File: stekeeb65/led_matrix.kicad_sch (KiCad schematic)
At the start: 68 parts

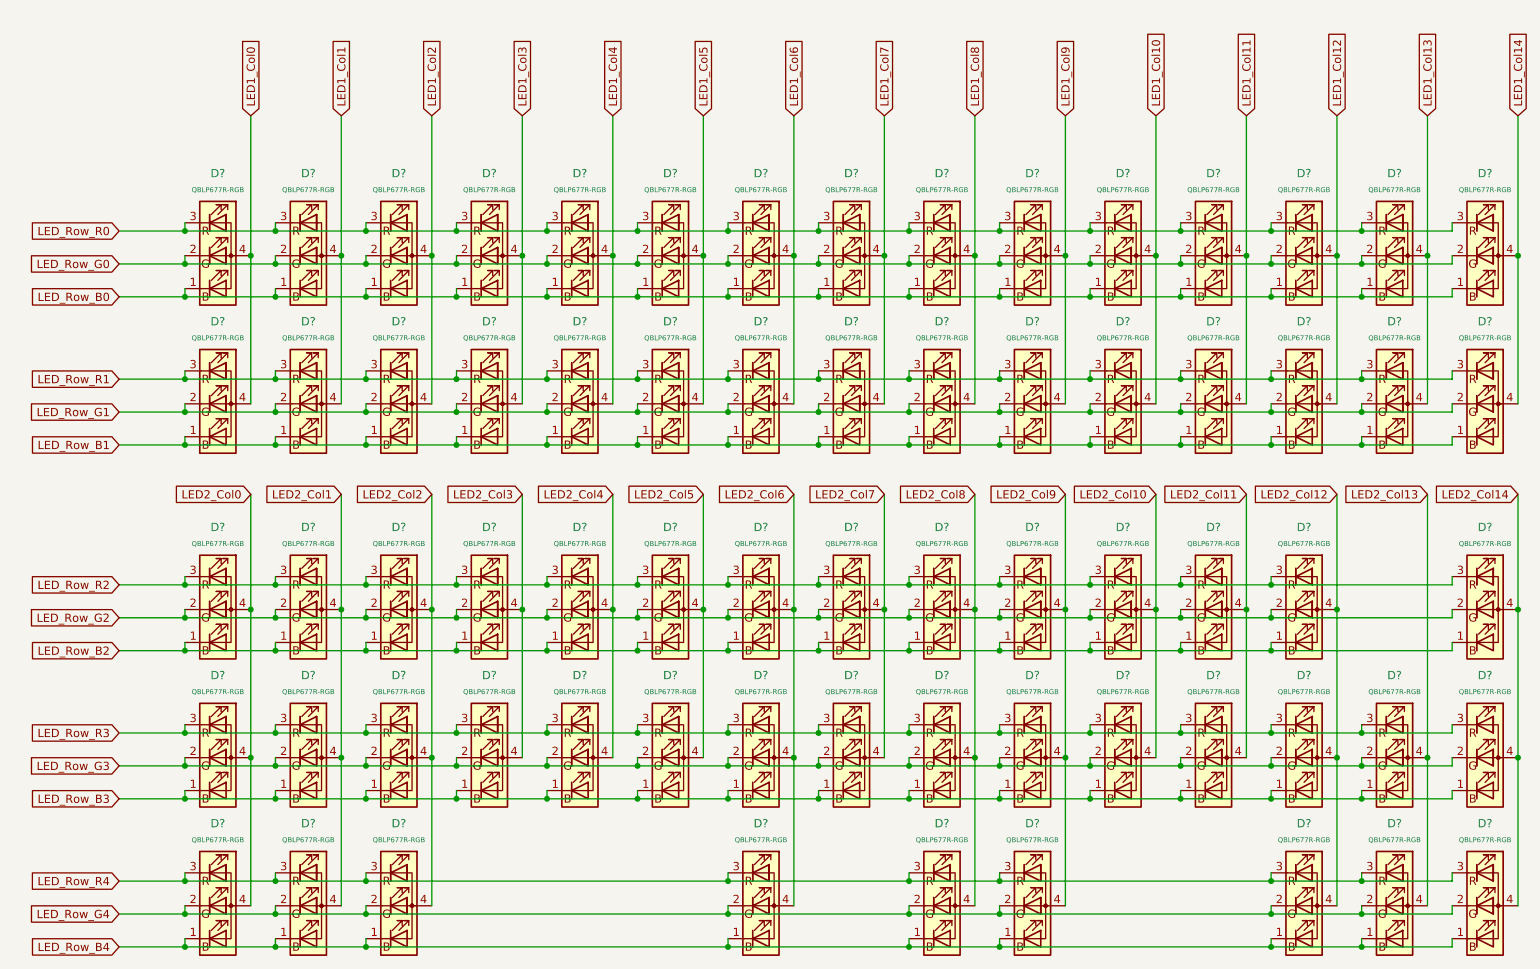
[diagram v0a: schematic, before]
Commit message: Adding keyboard footprints
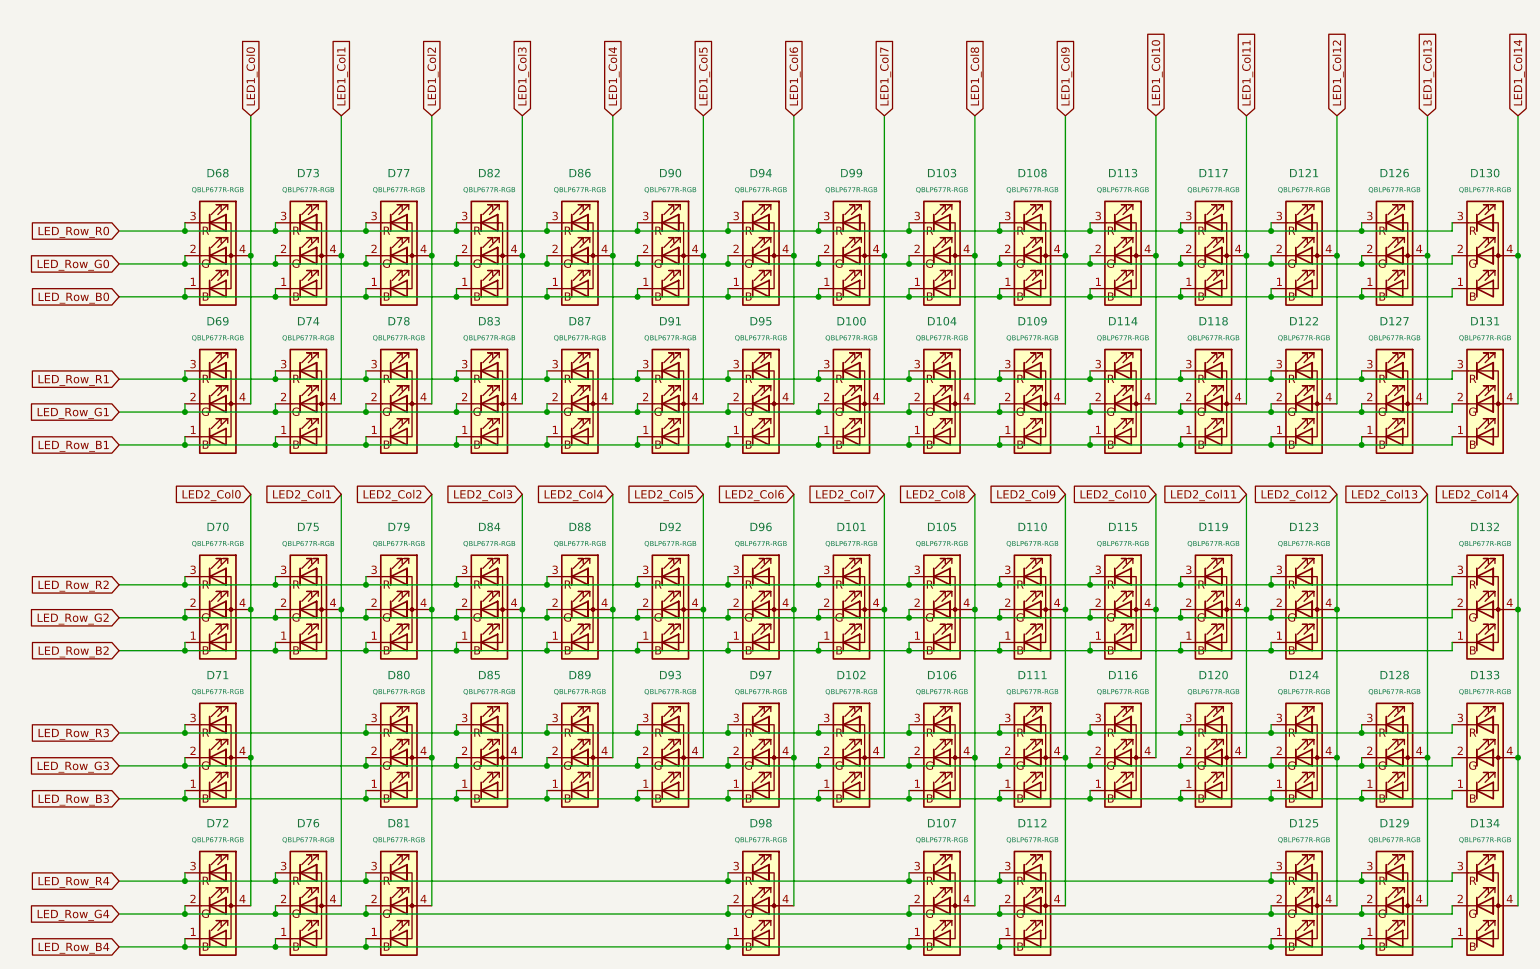
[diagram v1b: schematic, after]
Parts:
- removed D?: QBLP677R-RGB, symbol Device:LED_BGRA
- D100, D101, D102, D103, D104, D105, D106, D107, D108, D109, D110, D111, D112, D113, D114, D115, D116, D117, D118, D119, D120, D121, D122, D123, D124, D125, D126, D127, D128, D129, D130, D131, D132, D133, D134, D68, D69, D70, D71, D72, D73, D74, D75, D76, D77, D78, D79, D80, D81, D82, D83, D84, D85, D86, D87, D88, D89, D90, D91, D92, D93, D94, D95, D96, D97, D98, D99: renamed from D?; footprint (none) -> SamacSys_Parts:QBLP677R-RGB

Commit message: Committing before changes to PCB
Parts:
- D100, D101, D102, D103, D104, D105, D106, D107, D108, D109, D110, D111, D112, D113, D114, D115, D116, D117, D118, D119, D120, D121, D122, D123, D124, D125, D126, D127, D128, D129, D130, D131, D132, D133, D134, D68, D69, D70, D71, D72, D73, D74, D75, D76, D77, D78, D79, D80, D81, D82, D83, D84, D85, D86, D87, D88, D89, D90, D91, D92, D93, D94, D95, D96, D97, D98, D99: footprint SamacSys_Parts:QBLP677R-RGB -> random-keyboard-parts:QBLP677R-RGB

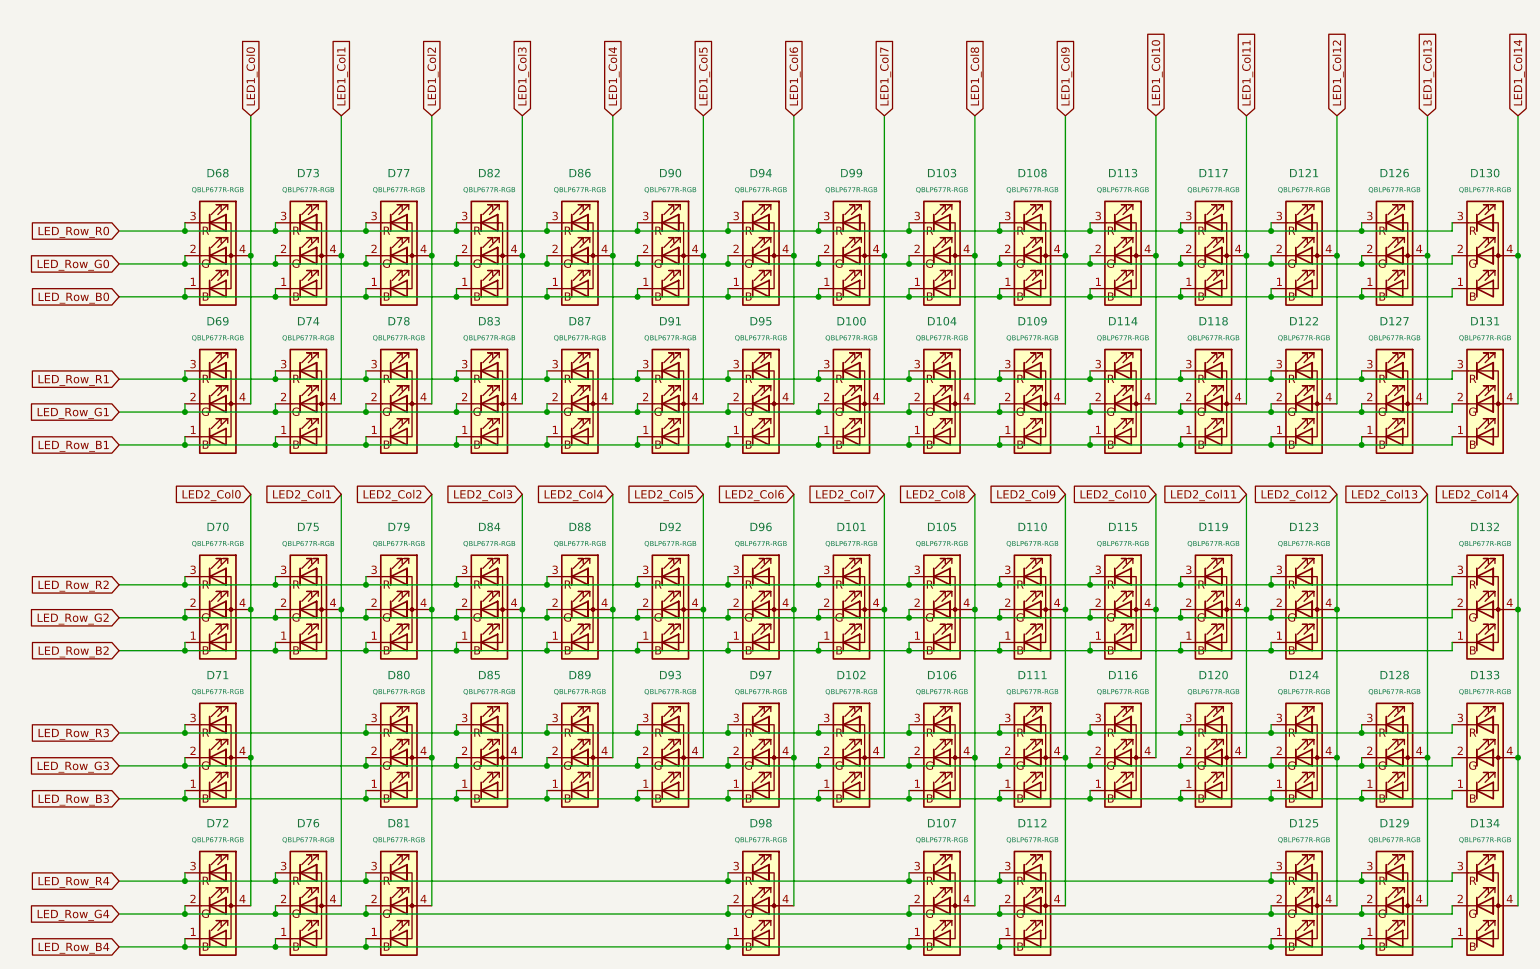
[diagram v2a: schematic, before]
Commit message: Adding key layout with leds
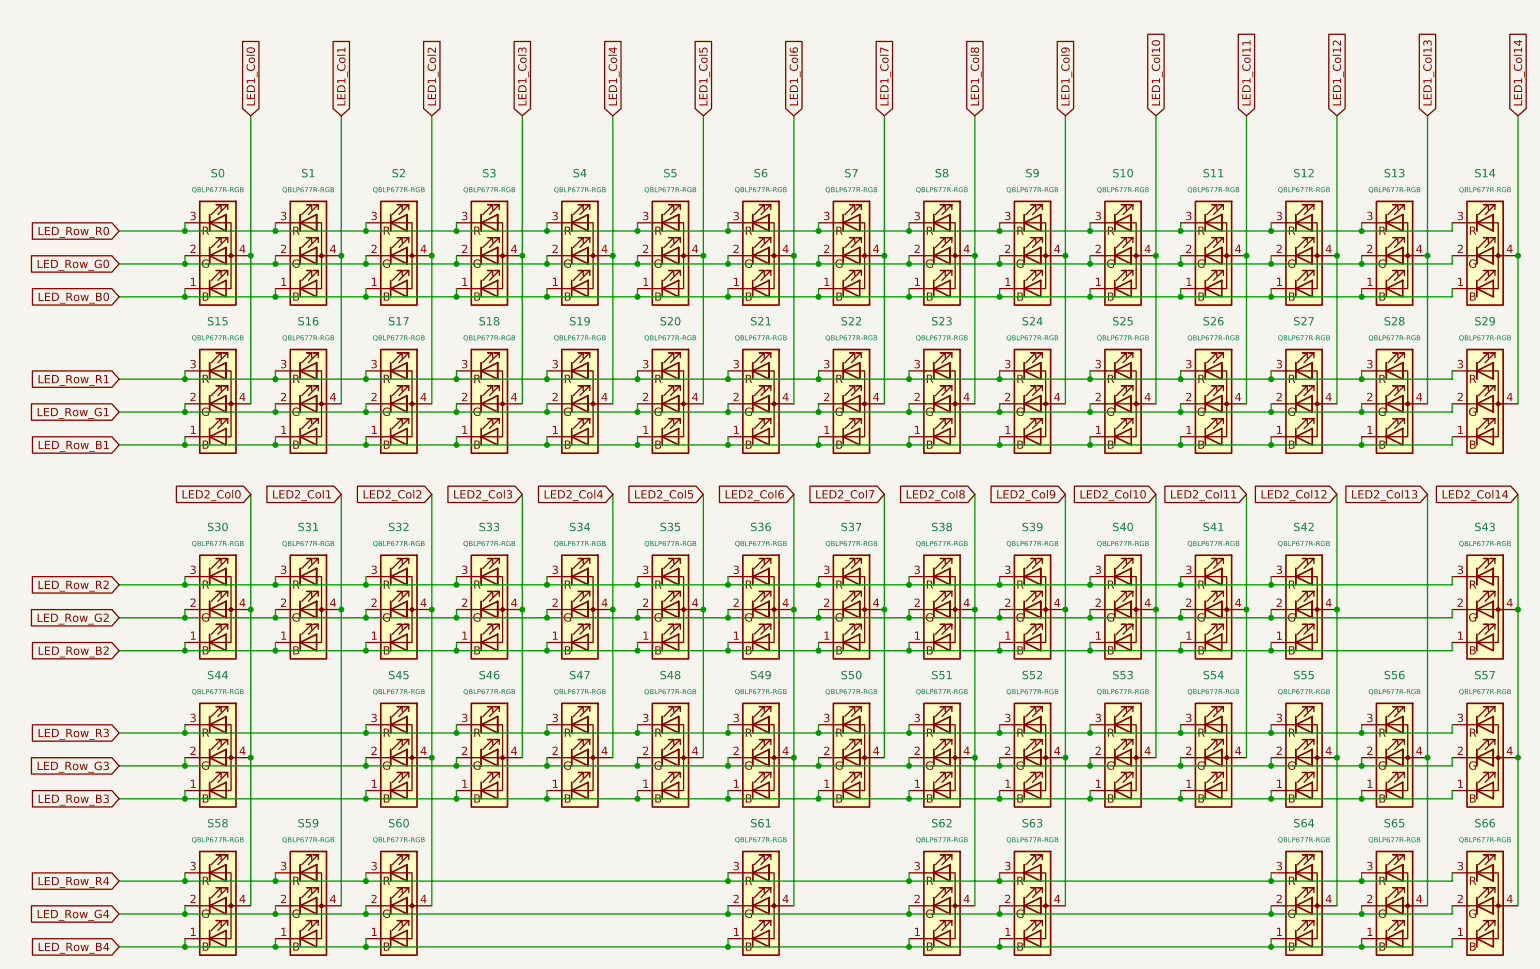
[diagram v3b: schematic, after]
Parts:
- renumbered D68 to S0, D73 to S1, D113 to S10, D117 to S11, D121 to S12, D126 to S13, D130 to S14, D69 to S15, D74 to S16, D78 to S17, D83 to S18, D87 to S19, D77 to S2, D91 to S20, D95 to S21, D100 to S22, D104 to S23, D109 to S24, D114 to S25, D118 to S26, D122 to S27, D127 to S28, D131 to S29, D82 to S3, D70 to S30, D75 to S31, D79 to S32, D84 to S33, D88 to S34, D92 to S35, D96 to S36, D101 to S37, D105 to S38, D110 to S39, D86 to S4, D115 to S40, D119 to S41, D123 to S42, D132 to S43, D71 to S44, D80 to S45, D85 to S46, D89 to S47, D93 to S48, D97 to S49, D90 to S5, D102 to S50, D106 to S51, D111 to S52, D116 to S53, D120 to S54, D124 to S55, D128 to S56, D133 to S57, D72 to S58, D76 to S59, D94 to S6, D81 to S60, D98 to S61, D107 to S62, D112 to S63, D125 to S64, D129 to S65, D134 to S66, D99 to S7, D103 to S8, D108 to S9

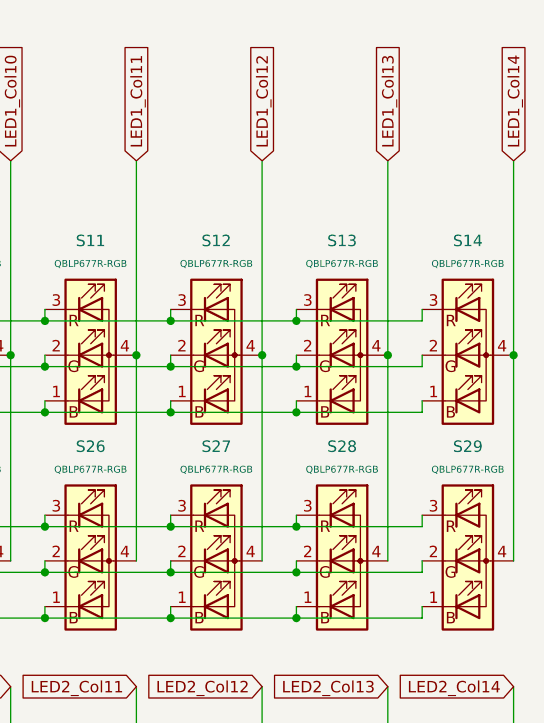
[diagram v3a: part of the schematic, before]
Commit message: Adding layout for diodes, LEDs, edge cuts
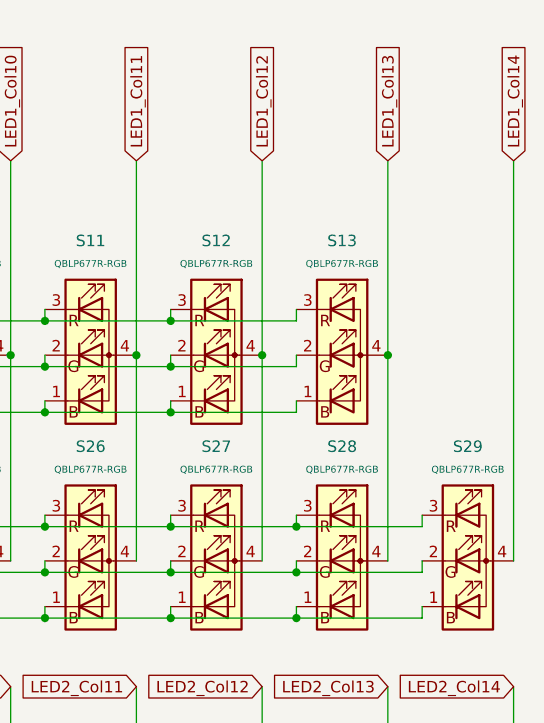
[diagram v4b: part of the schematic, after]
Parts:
- removed S14: QBLP677R-RGB, random-keyboard-parts:QBLP677R-RGB, symbol Device:LED_BGRA
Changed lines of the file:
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@@
   (junction (at 218.44 151.13) (diameter 0) (color 0 0 0 0)
   )
-  (junction (at 232.41 45.72) (diameter 0) (color 0 0 0 0)
-  )
   (junction (at 204.47 128.27) (diameter 0) (color 0 0 0 0)
   )
@@
   (junction (at 106.68 55.88) (diameter 0) (color 0 0 0 0)
   )
-  (junction (at 232.41 50.8) (diameter 0) (color 0 0 0 0)
-  )
   (junction (at 92.71 55.88) (diameter 0) (color 0 0 0 0)
   )
@@
   (junction (at 64.77 78.74) (diameter 0) (color 0 0 0 0)
   )
-  (junction (at 256.54 49.53) (diameter 0) (color 0 0 0 0)
-  )
   (junction (at 144.78 104.14) (diameter 0) (color 0 0 0 0)
   )
@@
   (junction (at 228.6 104.14) (diameter 0) (color 0 0 0 0)
   )
-  (junction (at 232.41 55.88) (diameter 0) (color 0 0 0 0)
-  )
   (junction (at 218.44 45.72) (diameter 0) (color 0 0 0 0)
   )
@@
     (stroke (width 0) (type default) (color 0 0 0 0))
   )
-  (wire (pts (xy 232.41 55.88) (xy 246.38 55.88))
-    (stroke (width 0) (type default) (color 0 0 0 0))
-  )
   (wire (pts (xy 176.53 128.27) (xy 190.5 128.27))
     (stroke (width 0) (type default) (color 0 0 0 0))
@@
     (stroke (width 0) (type default) (color 0 0 0 0))
   )
-  (wire (pts (xy 232.41 45.72) (xy 246.38 45.72))
-    (stroke (width 0) (type default) (color 0 0 0 0))
-  )
   (wire (pts (xy 106.68 123.19) (xy 106.68 121.92))
     (stroke (width 0) (type default) (color 0 0 0 0))
@@
     (stroke (width 0) (type default) (color 0 0 0 0))
   )
-  (wire (pts (xy 232.41 50.8) (xy 246.38 50.8))
-    (stroke (width 0) (type default) (color 0 0 0 0))
-  )
   (wire (pts (xy 204.47 55.88) (xy 218.44 55.88))
     (stroke (width 0) (type default) (color 0 0 0 0))
@@
     (stroke (width 0) (type default) (color 0 0 0 0))
   )
-  (wire (pts (xy 246.38 50.8) (xy 246.38 49.53))
-    (stroke (width 0) (type default) (color 0 0 0 0))
-  )
   (wire (pts (xy 134.62 49.53) (xy 134.62 50.8))
     (stroke (width 0) (type default) (color 0 0 0 0))
@@
     (stroke (width 0) (type default) (color 0 0 0 0))
   )
-  (wire (pts (xy 256.54 49.53) (xy 256.54 72.39))
+  (wire (pts (xy 256.54 27.94) (xy 256.54 72.39))
     (stroke (width 0) (type default) (color 0 0 0 0))
   )
@@
     (stroke (width 0) (type default) (color 0 0 0 0))
   )
-  (wire (pts (xy 256.54 27.94) (xy 256.54 49.53))
-    (stroke (width 0) (type default) (color 0 0 0 0))
-  )
   (wire (pts (xy 190.5 123.19) (xy 204.47 123.19))
     (stroke (width 0) (type default) (color 0 0 0 0))
@@
     (stroke (width 0) (type default) (color 0 0 0 0))
   )
-  (wire (pts (xy 246.38 55.88) (xy 246.38 54.61))
-    (stroke (width 0) (type default) (color 0 0 0 0))
-  )
   (wire (pts (xy 102.87 49.53) (xy 102.87 72.39))
     (stroke (width 0) (type default) (color 0 0 0 0))
@@
   )
   (wire (pts (xy 88.9 127) (xy 88.9 149.86))
-    (stroke (width 0) (type default) (color 0 0 0 0))
-  )
-  (wire (pts (xy 246.38 45.72) (xy 246.38 44.45))
     (stroke (width 0) (type default) (color 0 0 0 0))
   )
@@
       (effects (font (size 1.27 1.27)) hide)
     )
-    (pin "1")
-    (pin "2")
-    (pin "3")
-    (pin "4")
-  )
-  (symbol (lib_id "Device:LED_BGRA") (at 251.46 49.53 0) (unit 1)
-    (in_bom yes) (on_board yes) (fields_autoplaced)
-    (property "Reference" "S14" (id 0) (at 251.46 36.83 0))
-    (property "Value" "QBLP677R-RGB" (id 1) (at 251.46 39.37 0)
-      (effects (font (size 0.762 0.762)))
-    )
-    (property "Footprint" "random-keyboard-parts:QBLP677R-RGB" (id 2) (at 251.46 50.8 0)
-      (effects (font (size 1.27 1.27)) hide)
-    )
-    (property "Datasheet" "~" (id 3) (at 251.46 50.8 0)
-      (effects (font (size 1.27 1.27)) hide)
-    )

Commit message: Started layout for keyboard. still need to verify LED driver schematic
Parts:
- S0, S1, S10, S11, S12, S13, S15, S16, S17, S18, S19, S2, S20, S21, S22, S23, S24, S25, S26, S27, S28, S29, S3, S30, S31, S32, S33, S34, S35, S36, S37, S38, S39, S4, S40, S41, S42, S43, S44, S45, S46, S47, S48, S49, S5, S50, S51, S52, S53, S54, S55, S56, S57, S58, S59, S6, S60, S61, S62, S63, S64, S65, S66, S7, S8, S9: footprint random-keyboard-parts:QBLP677R-RGB -> random-keyboard-parts:QBLP677R-RGB-square_cutout

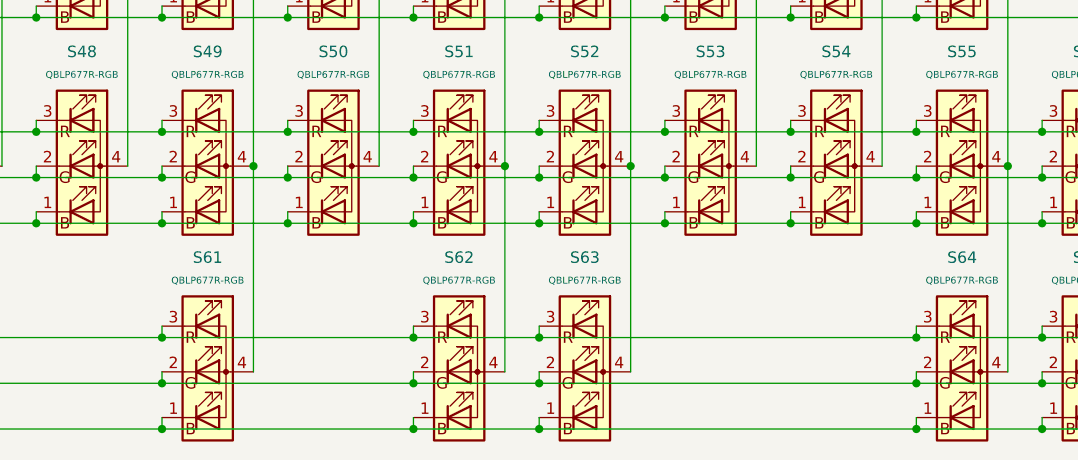
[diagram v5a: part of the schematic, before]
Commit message: Redoing keyboard layout. Adding flex cuts to PCB
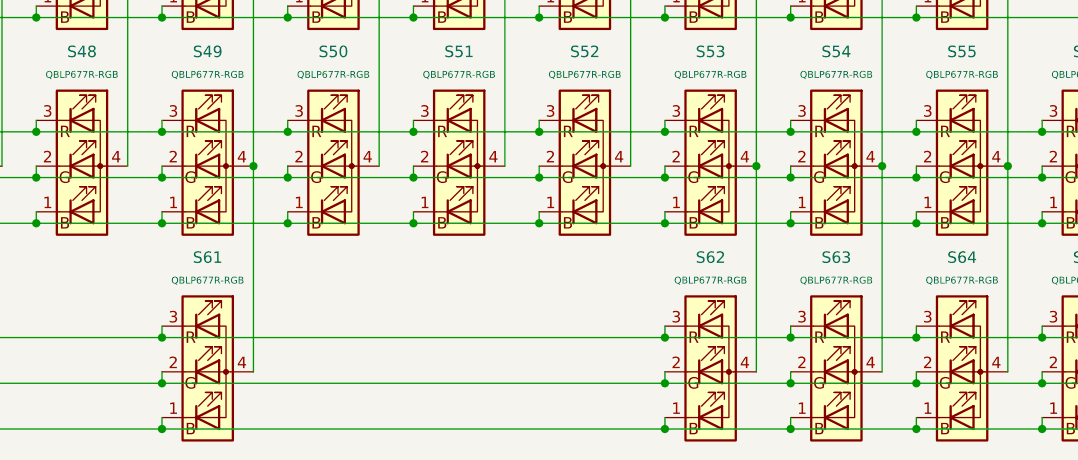
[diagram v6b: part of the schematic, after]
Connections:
- net LED2_Col10: now also S62.4 (A)
- net LED2_Col11: now also S63.4 (A)
- net LED2_Col8: no longer S62.4 (A)
- net LED2_Col9: no longer S63.4 (A)
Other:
- moved on the sheet: S62, S63
